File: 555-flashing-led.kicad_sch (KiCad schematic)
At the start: 3 parts, among them U1 7555

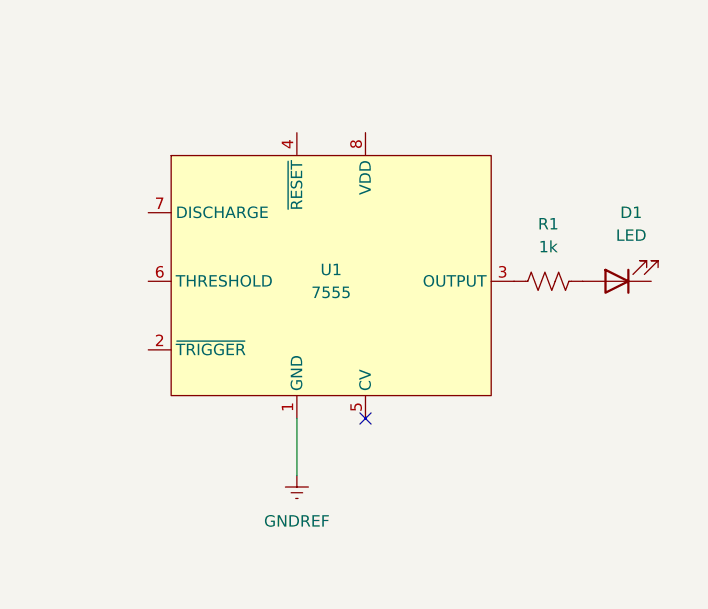
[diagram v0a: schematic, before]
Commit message: create schematic diagram; add reference in README
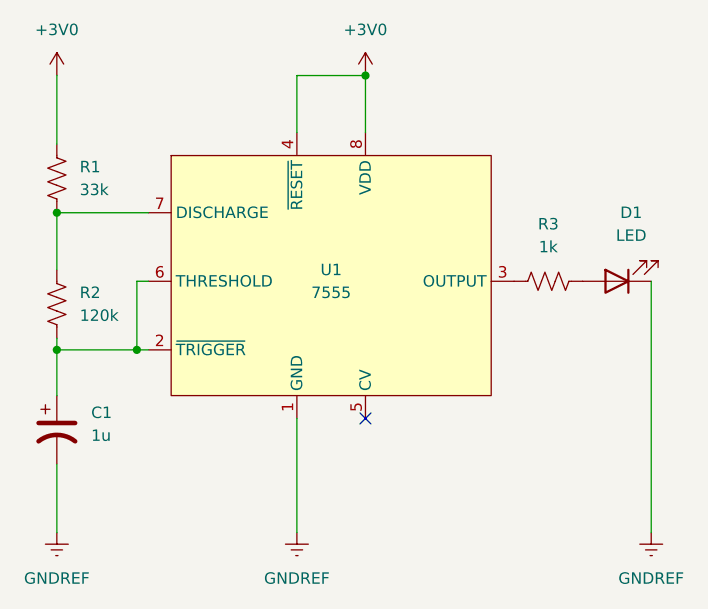
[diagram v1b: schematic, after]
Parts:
- added C1: 1u, symbol Device:C_Polarized_US
- added R1: 33k, symbol Device:R_US
- added R2: 120k, symbol Device:R_US
- renumbered R1 to R3
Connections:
- net GNDREF: now also D1.1 (K), C1.2
- net at U1.2 (~{TRIGGER}): now also U1.6 (THRESHOLD), C1.1, R2.2
- net +3V0: now reaches U1.4 (~{RESET})
- net +3V0: now also U1.8 (VDD), R1.2
- net at U1.7 (DISCHARGE): now also R1.1, R2.1
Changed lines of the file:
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@@
     (comment 4 "Author: Giovanni Dejan")
   )
+  (junction (at 125.73 62.23) (diameter 0) (color 0 0 0 0)
+  )
+  (junction (at 100.33 92.71) (diameter 0) (color 0 0 0 0)
+  )
+  (junction (at 91.44 77.47) (diameter 0) (color 0 0 0 0)
+  )
+  (junction (at 91.44 92.71) (diameter 0) (color 0 0 0 0)
+  )
   (no_connect (at 125.73 100.33))
-  (wire (pts (xy 118.11 106.68) (xy 118.11 100.33))
-    (stroke (width 0) (type default))
+  (wire (pts (xy 100.33 92.71) (xy 101.6 92.71))
+    (stroke (width 0) (type default))
+  )
+  (wire (pts (xy 91.44 62.23) (xy 91.44 69.85))
+    (stroke (width 0) (type default))
+  )
+  (wire (pts (xy 100.33 85.09) (xy 101.6 85.09))
+    (stroke (width 0) (type default))
+  )
+  (wire (pts (xy 125.73 62.23) (xy 125.73 68.58))
+    (stroke (width 0) (type default))
+  )
+  (wire (pts (xy 91.44 77.47) (xy 101.6 77.47))
+    (stroke (width 0) (type default))
+  )
+  (wire (pts (xy 118.11 62.23) (xy 118.11 68.58))
+    (stroke (width 0) (type default))
+  )
+  (wire (pts (xy 157.48 85.09) (xy 157.48 113.03))
+    (stroke (width 0) (type default))
+  )
+  (wire (pts (xy 91.44 92.71) (xy 91.44 97.79))
+    (stroke (width 0) (type default))
+  )
+  (wire (pts (xy 118.11 62.23) (xy 125.73 62.23))
+    (stroke (width 0) (type default))
+  )
+  (wire (pts (xy 91.44 105.41) (xy 91.44 113.03))
+    (stroke (width 0) (type default))
+  )
+  (wire (pts (xy 91.44 83.82) (xy 91.44 77.47))
+    (stroke (width 0) (type default))
+  )
+  (wire (pts (xy 100.33 85.09) (xy 100.33 92.71))
+    (stroke (width 0) (type default))
+  )
+  (wire (pts (xy 118.11 113.03) (xy 118.11 100.33))
+    (stroke (width 0) (type default))
+  )
+  (wire (pts (xy 91.44 92.71) (xy 100.33 92.71))
+    (stroke (width 0) (type default))
+  )
+  (wire (pts (xy 91.44 91.44) (xy 91.44 92.71))
+    (stroke (width 0) (type default))
+  )
+  (symbol (lib_id "Device:R_US") (at 91.44 87.63 0) (unit 1)
+    (in_bom yes) (on_board yes) (dnp no) (fields_autoplaced)
+    (property "Reference" "R2" (at 93.98 86.36 0)
+      (effects (font (size 1.27 1.27)) (justify left))
+    )
+    (property "Value" "120k" (at 93.98 88.9 0)
+      (effects (font (size 1.27 1.27)) (justify left))
+    )
+    (property "Footprint" "" (at 92.456 87.884 90)
+      (effects (font (size 1.27 1.27)) hide)
+    )
+    (property "Datasheet" "~" (at 91.44 87.63 0)
+      (effects (font (size 1.27 1.27)) hide)
+    )
+    (pin "1")
+    (pin "2")
+    (instances
+      (project "555-flashing-led"
+        (path "/22b5d8b2-f6b9-4aff-bf5b-a72462cf59e7"
+          (reference "R2") (unit 1)
+        )
+      )
+    )
   )
   (symbol (lib_id "Local_Library:7555") (at 121.92 85.09 0) (unit 1)
@@
     )
   )
+  (symbol (lib_id "Device:C_Polarized_US") (at 91.44 101.6 0) (unit 1)
+    (in_bom yes) (on_board yes) (dnp no) (fields_autoplaced)
+    (property "Reference" "C1" (at 95.25 99.695 0)
+      (effects (font (size 1.27 1.27)) (justify left))
+    )
+    (property "Value" "1u" (at 95.25 102.235 0)
+      (effects (font (size 1.27 1.27)) (justify left))
+    )
+    (property "Footprint" "" (at 91.44 101.6 0)
+      (effects (font (size 1.27 1.27)) hide)
+    )
+    (property "Datasheet" "~" (at 91.44 101.6 0)
+      (effects (font (size 1.27 1.27)) hide)
+    )
+    (pin "1")
+    (pin "2")
+    (instances
+      (project "555-flashing-led"
+        (path "/22b5d8b2-f6b9-4aff-bf5b-a72462cf59e7"
+          (reference "C1") (unit 1)
+        )
+      )
+    )
+  )
+  (symbol (lib_id "power:+3V0") (at 125.73 62.23 0) (unit 1)
+    (in_bom yes) (on_board yes) (dnp no) (fields_autoplaced)
+    (property "Reference" "#PWR02" (at 125.73 66.04 0)
+      (effects (font (size 1.27 1.27)) hide)
+    )
+    (property "Value" "+3V0" (at 125.73 57.15 0)
+      (effects (font (size 1.27 1.27)))
+    )
+    (property "Footprint" "" (at 125.73 62.23 0)
+      (effects (font (size 1.27 1.27)) hide)
+    )
+    (property "Datasheet" "" (at 125.73 62.23 0)
+      (effects (font (size 1.27 1.27)) hide)
+    )
+    (pin "1")
+    (instances
+      (project "555-flashing-led"
+        (path "/22b5d8b2-f6b9-4aff-bf5b-a72462cf59e7"
+          (reference "#PWR02") (unit 1)
+        )
+      )
+    )
+  )
   (symbol (lib_id "Device:LED") (at 153.67 85.09 180) (unit 1)
     (in_bom yes) (on_board yes) (dnp no) (fields_autoplaced)
@@
     )
   )
-  (symbol (lib_id "power:GNDREF") (at 118.11 106.68 0) (unit 1)
-    (in_bom yes) (on_board yes) (dnp no) (fields_autoplaced)
-    (property "Reference" "#PWR01" (at 118.11 113.03 0)
-      (effects (font (size 1.27 1.27)) hide)
-    )
-    (property "Value" "GNDREF" (at 118.11 111.76 0)
-      (effects (font (size 1.27 1.27)))
-    )
-    (property "Footprint" "" (at 118.11 106.68 0)
-      (effects (font (size 1.27 1.27)) hide)
-    )
-    (property "Datasheet" "" (at 118.11 106.68 0)
+  (symbol (lib_id "power:GNDREF") (at 157.48 113.03 0) (unit 1)
+    (in_bom yes) (on_board yes) (dnp no) (fields_autoplaced)
+    (property "Reference" "#PWR04" (at 157.48 119.38 0)
+      (effects (font (size 1.27 1.27)) hide)
+    )
+    (property "Value" "GNDREF" (at 157.48 118.11 0)
+      (effects (font (size 1.27 1.27)))
+    )
+    (property "Footprint" "" (at 157.48 113.03 0)
+      (effects (font (size 1.27 1.27)) hide)
+    )
+    (property "Datasheet" "" (at 157.48 113.03 0)
+      (effects (font (size 1.27 1.27)) hide)
+    )
+    (pin "1")
+    (instances
+      (project "555-flashing-led"
+        (path "/22b5d8b2-f6b9-4aff-bf5b-a72462cf59e7"
+          (reference "#PWR04") (unit 1)
+        )
+      )
+    )
+  )
+  (symbol (lib_id "power:GNDREF") (at 118.11 113.03 0) (unit 1)
+    (in_bom yes) (on_board yes) (dnp no) (fields_autoplaced)
+    (property "Reference" "#PWR01" (at 118.11 119.38 0)
+      (effects (font (size 1.27 1.27)) hide)
+    )
+    (property "Value" "GNDREF" (at 118.11 118.11 0)
+      (effects (font (size 1.27 1.27)))
+    )
+    (property "Footprint" "" (at 118.11 113.03 0)
+      (effects (font (size 1.27 1.27)) hide)
+    )
+    (property "Datasheet" "" (at 118.11 113.03 0)
       (effects (font (size 1.27 1.27)) hide)
     )
@@
     )
   )
+  (symbol (lib_id "power:GNDREF") (at 91.44 113.03 0) (unit 1)
+    (in_bom yes) (on_board yes) (dnp no) (fields_autoplaced)
+    (property "Reference" "#PWR05" (at 91.44 119.38 0)
+      (effects (font (size 1.27 1.27)) hide)
+    )
+    (property "Value" "GNDREF" (at 91.44 118.11 0)
+      (effects (font (size 1.27 1.27)))
+    )
+    (property "Footprint" "" (at 91.44 113.03 0)
+      (effects (font (size 1.27 1.27)) hide)
+    )
+    (property "Datasheet" "" (at 91.44 113.03 0)
+      (effects (font (size 1.27 1.27)) hide)
+    )
+    (pin "1")
+    (instances
+      (project "555-flashing-led"
+        (path "/22b5d8b2-f6b9-4aff-bf5b-a72462cf59e7"
+          (reference "#PWR05") (unit 1)
+        )
+      )
+    )
+  )
+  (symbol (lib_id "power:+3V0") (at 91.44 62.23 0) (unit 1)
+    (in_bom yes) (on_board yes) (dnp no) (fields_autoplaced)
+    (property "Reference" "#PWR03" (at 91.44 66.04 0)
+      (effects (font (size 1.27 1.27)) hide)
+    )
+    (property "Value" "+3V0" (at 91.44 57.15 0)
+      (effects (font (size 1.27 1.27)))
+    )
+    (property "Footprint" "" (at 91.44 62.23 0)
+      (effects (font (size 1.27 1.27)) hide)
+    )
+    (property "Datasheet" "" (at 91.44 62.23 0)
+      (effects (font (size 1.27 1.27)) hide)
+    )
+    (pin "1")
+    (instances
+      (project "555-flashing-led"
+        (path "/22b5d8b2-f6b9-4aff-bf5b-a72462cf59e7"
+          (reference "#PWR03") (unit 1)
+        )
+      )
+    )
+  )
+  (symbol (lib_id "Device:R_US") (at 91.44 73.66 180) (unit 1)
+    (in_bom yes) (on_board yes) (dnp no) (fields_autoplaced)
+    (property "Reference" "R1" (at 93.98 72.39 0)
+      (effects (font (size 1.27 1.27)) (justify right))
+    )
+    (property "Value" "33k" (at 93.98 74.93 0)
+      (effects (font (size 1.27 1.27)) (justify right))
+    )
+    (property "Footprint" "" (at 90.424 73.406 90)
+      (effects (font (size 1.27 1.27)) hide)
+    )
+    (property "Datasheet" "~" (at 91.44 73.66 0)
+      (effects (font (size 1.27 1.27)) hide)
+    )
+    (pin "1")
+    (pin "2")
+    (instances
+      (project "555-flashing-led"
+        (path "/22b5d8b2-f6b9-4aff-bf5b-a72462cf59e7"
+          (reference "R1") (unit 1)
+        )
+      )
+    )
+  )
   (symbol (lib_id "Device:R_US") (at 146.05 85.09 90) (unit 1)
     (in_bom yes) (on_board yes) (dnp no) (fields_autoplaced)
-    (property "Reference" "R1" (at 146.05 78.74 90)
+    (property "Reference" "R3" (at 146.05 78.74 90)
       (effects (font (size 1.27 1.27)))
     )
@@
       (project "555-flashing-led"
         (path "/22b5d8b2-f6b9-4aff-bf5b-a72462cf59e7"
-          (reference "R1") (unit 1)
-        )
-      )
+          (reference "R3") (unit 1)
+        )
+      )

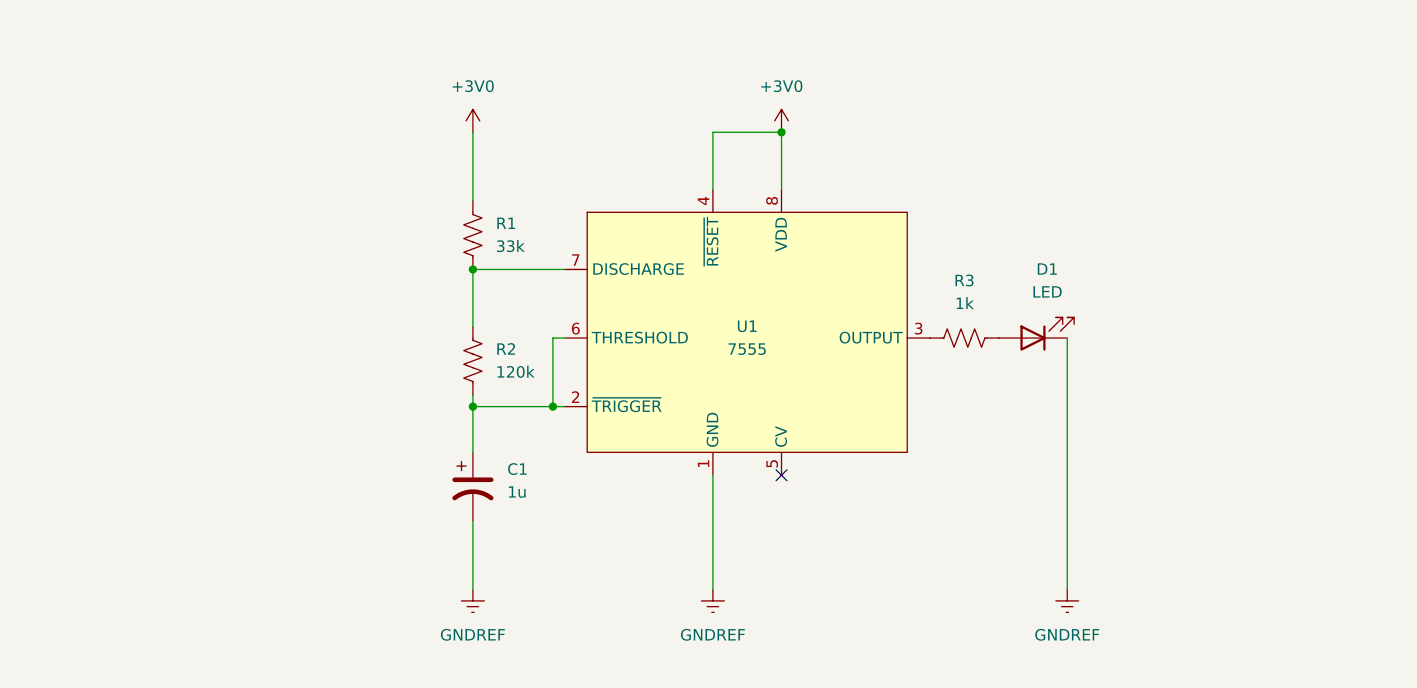
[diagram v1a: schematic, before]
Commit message: use footprint from library
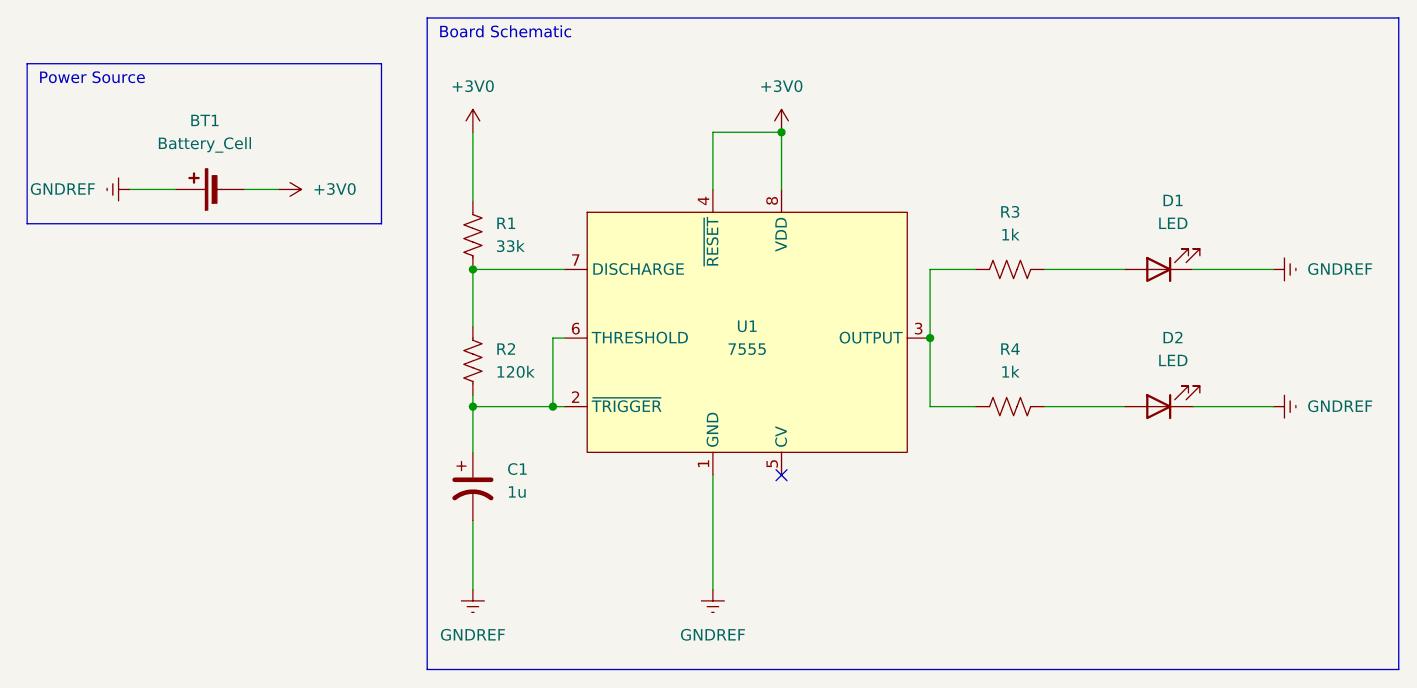
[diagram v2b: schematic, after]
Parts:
- added BT1: Battery_Cell, Battery:BatteryHolder_Keystone_107_1x23mm, symbol Device:Battery_Cell
- added D2: LED, LED_THT:LED_D5.0mm, symbol Device:LED
- added R4: 1k, Resistor_THT:R_Axial_DIN0309_L9.0mm_D3.2mm_P15.24mm_Horizontal, symbol Device:R_US
- C1: footprint (none) -> Capacitor_THT:CP_Radial_D5.0mm_P2.50mm
- D1: footprint (none) -> LED_THT:LED_D5.0mm
- R1, R2, R3: footprint (none) -> Resistor_THT:R_Axial_DIN0309_L9.0mm_D3.2mm_P15.24mm_Horizontal
- U1: footprint (none) -> Package_DIP:DIP-8_W7.62mm_LongPads
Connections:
- net +3V0: now also BT1.2 (-)
- net GNDREF: now also BT1.1 (+), D2.1 (K)
- net at R3.1, U1.3 (OUTPUT): now also R4.1
- new net: D2.2 (A), R4.2
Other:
- note added: "Board Schematic"
- note added: "Power Source"
- moved on the sheet: D1, R3

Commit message: finalize pcb
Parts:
- R3, R4: value 1k -> 100
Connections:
- net +3V0: now also BT1.1 (+); no longer BT1.2 (-)
- net GNDREF: now also BT1.2 (-); no longer BT1.1 (+)
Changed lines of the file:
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@@
     (stroke (width 0) (type default))
   )
-  (rectangle (start 41.91 54.61) (end 81.28 72.39)
+  (rectangle (start 43.18 54.61) (end 82.55 72.39)
     (stroke (width 0) (type default))
     (fill (type none))
@@
     (effects (font (size 1.27 1.27)) (justify left bottom))
   )
-  (text "Power Source" (at 43.18 57.15 0)
+  (text "Power Source" (at 44.45 57.15 0)
     (effects (font (size 1.27 1.27)) (justify left bottom))
   )
@@
     )
   )
+  (symbol (lib_id "power:GNDREF") (at 69.85 68.58 90) (unit 1)
+    (in_bom yes) (on_board yes) (dnp no) (fields_autoplaced)
+    (property "Reference" "#PWR07" (at 76.2 68.58 0)
+      (effects (font (size 1.27 1.27)) hide)
+    )
+    (property "Value" "GNDREF" (at 73.66 68.58 90)
+      (effects (font (size 1.27 1.27)) (justify right))
+    )
+    (property "Footprint" "" (at 69.85 68.58 0)
+      (effects (font (size 1.27 1.27)) hide)
+    )
+    (property "Datasheet" "" (at 69.85 68.58 0)
+      (effects (font (size 1.27 1.27)) hide)
+    )
+    (pin "1")
+    (instances
+      (project "555-flashing-led"
+        (path "/22b5d8b2-f6b9-4aff-bf5b-a72462cf59e7"
+          (reference "#PWR07") (unit 1)
+        )
+      )
+    )
+  )
   (symbol (lib_id "Device:R_US") (at 151.13 92.71 90) (unit 1)
     (in_bom yes) (on_board yes) (dnp no) (fields_autoplaced)
@@
       (effects (font (size 1.27 1.27)))
     )
-    (property "Value" "1k" (at 151.13 88.9 90)
+    (property "Value" "100" (at 151.13 88.9 90)
       (effects (font (size 1.27 1.27)))
     )
@@
         (path "/22b5d8b2-f6b9-4aff-bf5b-a72462cf59e7"
           (reference "#PWR08") (unit 1)
+        )
+      )
+    )
+  )
+  (symbol (lib_id "power:+3V0") (at 53.34 68.58 90) (unit 1)
+    (in_bom yes) (on_board yes) (dnp no) (fields_autoplaced)
+    (property "Reference" "#PWR06" (at 57.15 68.58 0)
+      (effects (font (size 1.27 1.27)) hide)
+    )
+    (property "Value" "+3V0" (at 49.53 68.58 90)
+      (effects (font (size 1.27 1.27)) (justify left))
+    )
+    (property "Footprint" "" (at 53.34 68.58 0)
+      (effects (font (size 1.27 1.27)) hide)
+    )
+    (property "Datasheet" "" (at 53.34 68.58 0)
+      (effects (font (size 1.27 1.27)) hide)
+    )
+    (pin "1")
+    (instances
+      (project "555-flashing-led"
+        (path "/22b5d8b2-f6b9-4aff-bf5b-a72462cf59e7"
+          (reference "#PWR06") (unit 1)
         )
       )
@@
       (effects (font (size 1.27 1.27)))
     )
-    (property "Value" "1k" (at 151.13 73.66 90)
+    (property "Value" "100" (at 151.13 73.66 90)
       (effects (font (size 1.27 1.27)))
     )
@@
         )
       )
-    )
-  )
-  (symbol (lib_id "power:GNDREF") (at 53.34 68.58 270) (unit 1)
-    (in_bom yes) (on_board yes) (dnp no) (fields_autoplaced)
-    (property "Reference" "#PWR07" (at 46.99 68.58 0)
-      (effects (font (size 1.27 1.27)) hide)
-    )
-    (property "Value" "GNDREF" (at 49.53 68.58 90)
-      (effects (font (size 1.27 1.27)) (justify right))
-    )
-    (property "Footprint" "" (at 53.34 68.58 0)
-      (effects (font (size 1.27 1.27)) hide)
-    )
-    (property "Datasheet" "" (at 53.34 68.58 0)
-      (effects (font (size 1.27 1.27)) hide)
-    )
-    (pin "1")
-    (instances
-      (project "555-flashing-led"
-        (path "/22b5d8b2-f6b9-4aff-bf5b-a72462cf59e7"
-          (reference "#PWR07") (unit 1)
-        )
-      )
-    )
-  )
-  (symbol (lib_id "power:+3V0") (at 69.85 68.58 270) (unit 1)
-    (in_bom yes) (on_board yes) (dnp no) (fields_autoplaced)
-    (property "Reference" "#PWR06" (at 66.04 68.58 0)
-      (effects (font (size 1.27 1.27)) hide)
-    )
-    (property "Value" "+3V0" (at 73.66 68.58 90)
-      (effects (font (size 1.27 1.27)) (justify left))
-    )
-    (property "Footprint" "" (at 69.85 68.58 0)
-      (effects (font (size 1.27 1.27)) hide)
-    )
-    (property "Datasheet" "" (at 69.85 68.58 0)
-      (effects (font (size 1.27 1.27)) hide)
-    )
-    (pin "1")
-    (instances
-      (project "555-flashing-led"
-        (path "/22b5d8b2-f6b9-4aff-bf5b-a72462cf59e7"
-          (reference "#PWR06") (unit 1)
-        )
-      )

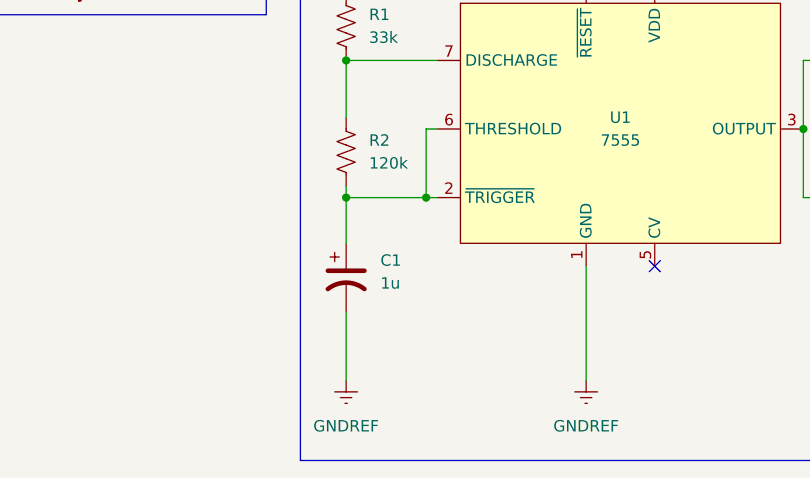
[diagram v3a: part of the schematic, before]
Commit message: update capacitors
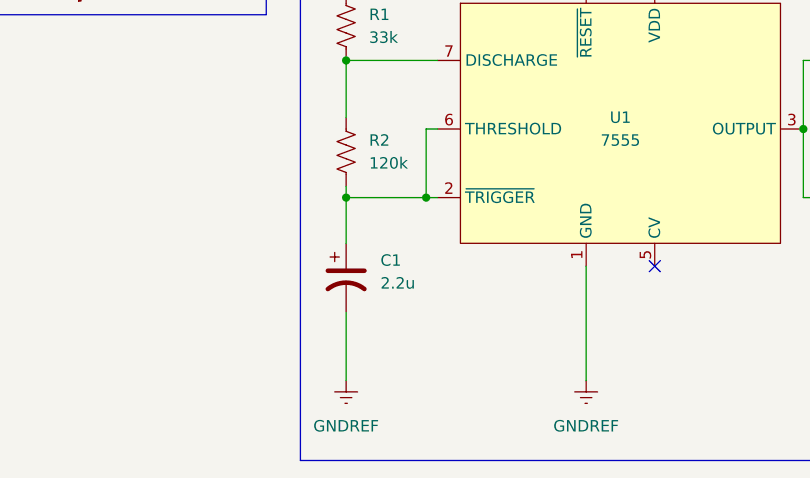
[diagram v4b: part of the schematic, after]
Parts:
- C1: value 1u -> 2.2u
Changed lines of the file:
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@@
       (effects (font (size 1.27 1.27)) (justify left))
     )
-    (property "Value" "1u" (at 95.25 102.235 0)
+    (property "Value" "2.2u" (at 95.25 102.235 0)
       (effects (font (size 1.27 1.27)) (justify left))
     )
